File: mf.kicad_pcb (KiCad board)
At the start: 2 copper layers, 280 x 130 mm, 18 parts

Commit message: New schematic
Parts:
- added C2: Capacitor_NP, Capacitor_THT:C_Disc_D3.0mm_W2.0mm_P2.50mm, F.Cu at (496.1, 239.6)
- added C3: Capacitor_NP, Capacitor_THT:C_Disc_D3.0mm_W2.0mm_P2.50mm, F.Cu at (496.1, 243.2)
- added C4: Capacitor_NP, Capacitor_THT:C_Disc_D3.0mm_W2.0mm_P2.50mm, F.Cu at (547.9, 225.9)
- added C6: Capacitor_NP, Capacitor_THT:C_Disc_D3.0mm_W2.0mm_P2.50mm, F.Cu at (547.9, 229.4)
- added R17: Resistor, Resistor_THT:R_Axial_DIN0207_L6.3mm_D2.5mm_P10.16mm_Horizontal, F.Cu at (482.8, 218.0)
- added R18: Resistor, Resistor_THT:R_Axial_DIN0207_L6.3mm_D2.5mm_P10.16mm_Horizontal, F.Cu at (482.8, 222.1)
- added R19: Resistor, Resistor_THT:R_Axial_DIN0207_L6.3mm_D2.5mm_P10.16mm_Horizontal, F.Cu at (482.8, 226.1)
- added R20: Resistor, Resistor_THT:R_Axial_DIN0207_L6.3mm_D2.5mm_P10.16mm_Horizontal, F.Cu at (482.8, 230.2)
- added R21: Resistor, Resistor_THT:R_Axial_DIN0207_L6.3mm_D2.5mm_P10.16mm_Horizontal, F.Cu at (482.8, 234.2)
- added R22: Resistor, Resistor_THT:R_Axial_DIN0207_L6.3mm_D2.5mm_P10.16mm_Horizontal, F.Cu at (482.8, 238.3)
- added R23: Resistor, Resistor_THT:R_Axial_DIN0207_L6.3mm_D2.5mm_P10.16mm_Horizontal, F.Cu at (482.8, 242.3)
- added R24: Resistor, Resistor_THT:R_Axial_DIN0207_L6.3mm_D2.5mm_P10.16mm_Horizontal, F.Cu at (482.8, 246.4)
- added R25: Resistor, Resistor_THT:R_Axial_DIN0207_L6.3mm_D2.5mm_P10.16mm_Horizontal, F.Cu at (482.8, 250.4)
- added R26: Resistor, Resistor_THT:R_Axial_DIN0207_L6.3mm_D2.5mm_P10.16mm_Horizontal, F.Cu at (482.8, 254.5)
- added R27: Resistor, Resistor_THT:R_Axial_DIN0207_L6.3mm_D2.5mm_P10.16mm_Horizontal, F.Cu at (482.8, 258.5)
- added R28: Resistor, Resistor_THT:R_Axial_DIN0207_L6.3mm_D2.5mm_P10.16mm_Horizontal, F.Cu at (482.8, 262.6)
- added R29: Resistor, Resistor_THT:R_Axial_DIN0207_L6.3mm_D2.5mm_P10.16mm_Horizontal, F.Cu at (482.8, 266.6)
- added R30: Resistor, Resistor_THT:R_Axial_DIN0207_L6.3mm_D2.5mm_P10.16mm_Horizontal, F.Cu at (482.8, 270.7)
- added R31: Resistor, Resistor_THT:R_Axial_DIN0207_L6.3mm_D2.5mm_P10.16mm_Horizontal, F.Cu at (482.8, 274.7)
- added R32: Resistor, Resistor_THT:R_Axial_DIN0207_L6.3mm_D2.5mm_P10.16mm_Horizontal, F.Cu at (482.8, 278.8)
- added R33: R, Resistor_THT:R_Axial_DIN0207_L6.3mm_D2.5mm_P10.16mm_Horizontal, F.Cu at (547.9, 218.0)
- added R37: R, Resistor_THT:R_Axial_DIN0207_L6.3mm_D2.5mm_P10.16mm_Horizontal, F.Cu at (547.9, 222.1)
- added U11: DM13a, Package_DIP:DIP-24_W10.16mm, F.Cu at (534.6, 218.0)
- added U5: 74HC165, Package_DIP:DIP-16_W7.62mm_LongPads, F.Cu at (496.5, 218.0)
- added U6: 74HC165, Package_DIP:DIP-16_W7.62mm_LongPads, F.Cu at (508.1, 218.0)
- added U9: DM13a, Package_DIP:DIP-24_W10.16mm, F.Cu at (521.3, 218.0)
- U1: value ~ -> Sparkfun_Pro_Micro
- U4: footprint mf:RP2040-Zero -> mf:7seg_x8
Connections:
- BC1 pad 2: unconnected-(BC1-C-Pad2) -> GND
- BC1 pad 3: unconnected-(BC1-NO-Pad3) -> Net-(BC1-NO)
- BC1 pad 4: unconnected-(BC1-LED-Pad4) -> /Input/LED_BC1
- BC1 pad 5: unconnected-(BC1-GND-Pad5) -> +5V
- BC2 pad 2: unconnected-(BC2-C-Pad2) -> GND
- BC2 pad 3: unconnected-(BC2-NO-Pad3) -> Net-(BC2-NO)
- BC2 pad 4: unconnected-(BC2-LED-Pad4) -> /Input/LED_BC2
- BC2 pad 5: unconnected-(BC2-GND-Pad5) -> +5V
- BC3 pad 2: unconnected-(BC3-C-Pad2) -> GND
- BC3 pad 3: unconnected-(BC3-NO-Pad3) -> Net-(BC3-NO)
- BC3 pad 4: unconnected-(BC3-LED-Pad4) -> /Input/LED_BC3
- BC3 pad 5: unconnected-(BC3-GND-Pad5) -> +5V
- BC4 pad 2: unconnected-(BC4-C-Pad2) -> GND
- BC4 pad 3: unconnected-(BC4-NO-Pad3) -> Net-(BC4-NO)
- BC4 pad 4: unconnected-(BC4-LED-Pad4) -> /Input/LED_BC4
- BC4 pad 5: unconnected-(BC4-GND-Pad5) -> +5V
- BC5 pad 2: unconnected-(BC5-C-Pad2) -> GND
- BC5 pad 3: unconnected-(BC5-NO-Pad3) -> Net-(BC5-NO)
- BC5 pad 4: unconnected-(BC5-LED-Pad4) -> /Input/LED_BC5
- BC5 pad 5: unconnected-(BC5-GND-Pad5) -> +5V
- BC6 pad 2: unconnected-(BC6-C-Pad2) -> GND
- BC6 pad 3: unconnected-(BC6-NO-Pad3) -> Net-(BC6-NO)
- BC6 pad 4: unconnected-(BC6-LED-Pad4) -> /Input/LED_BC6
- BC6 pad 5: unconnected-(BC6-GND-Pad5) -> +5V
- BC7 pad 2: unconnected-(BC7-C-Pad2) -> GND
- BC7 pad 3: unconnected-(BC7-NO-Pad3) -> Net-(BC7-NO)
- BC7 pad 4: unconnected-(BC7-LED-Pad4) -> /Input/LED_BC7
- BC7 pad 5: unconnected-(BC7-GND-Pad5) -> +5V
- E1 pad 1: unconnected-(E1-A-Pad1) -> /Input/E1_A
- E1 pad 2: unconnected-(E1-COM-Pad2) -> GND
- E1 pad 3: unconnected-(E1-B-Pad3) -> /Input/E1_B
- E1 pad 4: unconnected-(E1-D-Pad4) -> Net-(E1-D)
- E1 pad 5: unconnected-(E1-E-Pad5) -> GND
- E2 pad 1: unconnected-(E2-A-Pad1) -> /Input/E2_A
- E2 pad 2: unconnected-(E2-COM-Pad2) -> GND
- E2 pad 3: unconnected-(E2-B-Pad3) -> /Input/E2_B
- E2 pad 4: unconnected-(E2-D-Pad4) -> Net-(E2-D)
- E2 pad 5: unconnected-(E2-E-Pad5) -> GND
- E3 pad 1: unconnected-(E3-A-Pad1) -> /Input/E3_A
- E3 pad 2: unconnected-(E3-COM-Pad2) -> GND
- E3 pad 3: unconnected-(E3-B-Pad3) -> /Input/E3_B
- E3 pad 4: unconnected-(E3-D-Pad4) -> Net-(E3-D)
- E3 pad 5: unconnected-(E3-E-Pad5) -> GND
- E4 pad 1: unconnected-(E4-A-Pad1) -> /Input/E4_A
- E4 pad 2: unconnected-(E4-COM-Pad2) -> GND
- E4 pad 3: unconnected-(E4-B-Pad3) -> /Input/E4_B
- E4 pad 4: unconnected-(E4-D-Pad4) -> Net-(E4-D)
- E4 pad 5: unconnected-(E4-E-Pad5) -> GND
- RB1 pad 1: unconnected-(RB1-Pad1) -> GND
- RB1 pad 2: unconnected-(RB1-Pad2) -> Net-(U6-D3)
- RB2 pad 1: unconnected-(RB2-Pad1) -> GND
- RB2 pad 2: unconnected-(RB2-Pad2) -> Net-(U6-D2)
- RB3 pad 1: unconnected-(RB3-Pad1) -> GND
- RB3 pad 2: unconnected-(RB3-Pad2) -> Net-(U6-D1)
- U1 pad 3: unconnected-(U1-D2-Pad3) -> GND
- U1 pad 4: unconnected-(U1-GND-Pad4) -> GND
- U2 pad 1: unconnected-(U2-5V-Pad1) -> +5V
- U2 pad 2: unconnected-(U2-D1-Pad2) -> GND
- U2 pad 3: unconnected-(U2-D2-Pad3) -> /Output/O_8_DIN
- U2 pad 4: unconnected-(U2-GND-Pad4) -> /Output/O_8_CS
- U3 pad 1: unconnected-(U3-5V-Pad1) -> /Output/O_4_CLK
- U3 pad 10: unconnected-(U3-GP0-Pad10) -> (no net)
- U3 pad 11: unconnected-(U3-GP1-Pad11) -> (no net)
- U3 pad 12: unconnected-(U3-GP2-Pad12) -> (no net)
- U3 pad 13: unconnected-(U3-GP3-Pad13) -> (no net)
- U3 pad 14: unconnected-(U3-GP4-Pad14) -> (no net)
- U3 pad 15: unconnected-(U3-GP5-Pad15) -> (no net)
- U3 pad 16: unconnected-(U3-GP6-Pad16) -> (no net)
- U3 pad 17: unconnected-(U3-GP7-Pad17) -> (no net)
- U3 pad 18: unconnected-(U3-GP8-Pad18) -> (no net)
- U3 pad 19: unconnected-(U3-GP13-Pad19) -> (no net)
- U3 pad 2: unconnected-(U3-GND-Pad2) -> /Output/O_4_DIN
- U3 pad 20: unconnected-(U3-GP12-Pad20) -> (no net)
- U3 pad 21: unconnected-(U3-GP11-Pad21) -> (no net)
- U3 pad 22: unconnected-(U3-GP10-Pad22) -> (no net)
- U3 pad 23: unconnected-(U3-GP9-Pad23) -> (no net)
- U3 pad 3: unconnected-(U3-3V3-Pad3) -> +5V
- U3 pad 4: unconnected-(U3-GP29-Pad4) -> GND
- U3 pad 5: unconnected-(U3-GP28-Pad5) -> (no net)
- U3 pad 6: unconnected-(U3-GP27-Pad6) -> (no net)
- U3 pad 7: unconnected-(U3-GP26-Pad7) -> (no net)
- U3 pad 8: unconnected-(U3-GP15-Pad8) -> (no net)
- U3 pad 9: unconnected-(U3-GP14-Pad9) -> (no net)
- U4 pad 1: unconnected-(U4-5V-Pad1) -> +5V
- U4 pad 2: unconnected-(U4-GND-Pad2) -> GND
- U4 pad 3: unconnected-(U4-3V3-Pad3) -> Net-(U2-DOUT)
- U4 pad 4: unconnected-(U4-GP29-Pad4) -> Net-(U2-LODA)

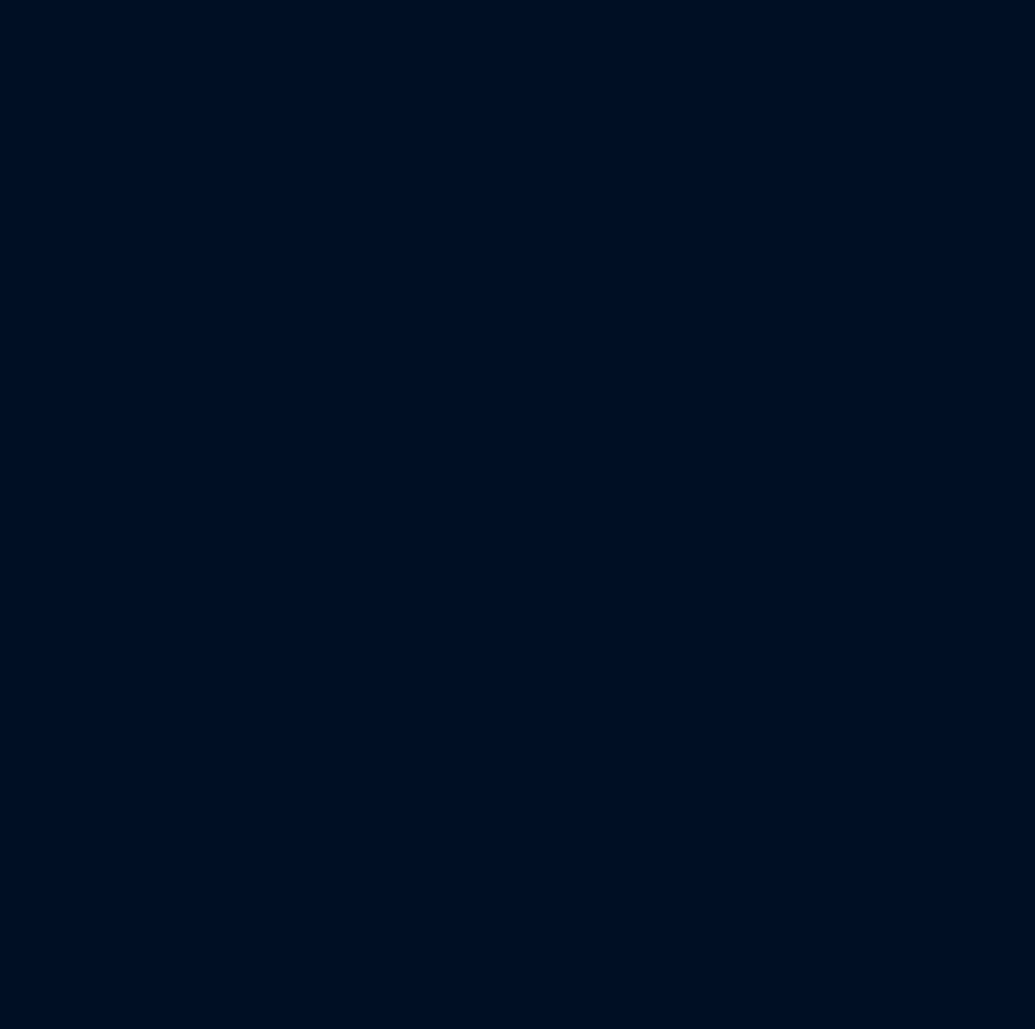
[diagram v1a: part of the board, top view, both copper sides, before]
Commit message: Update schematic with nearly everything
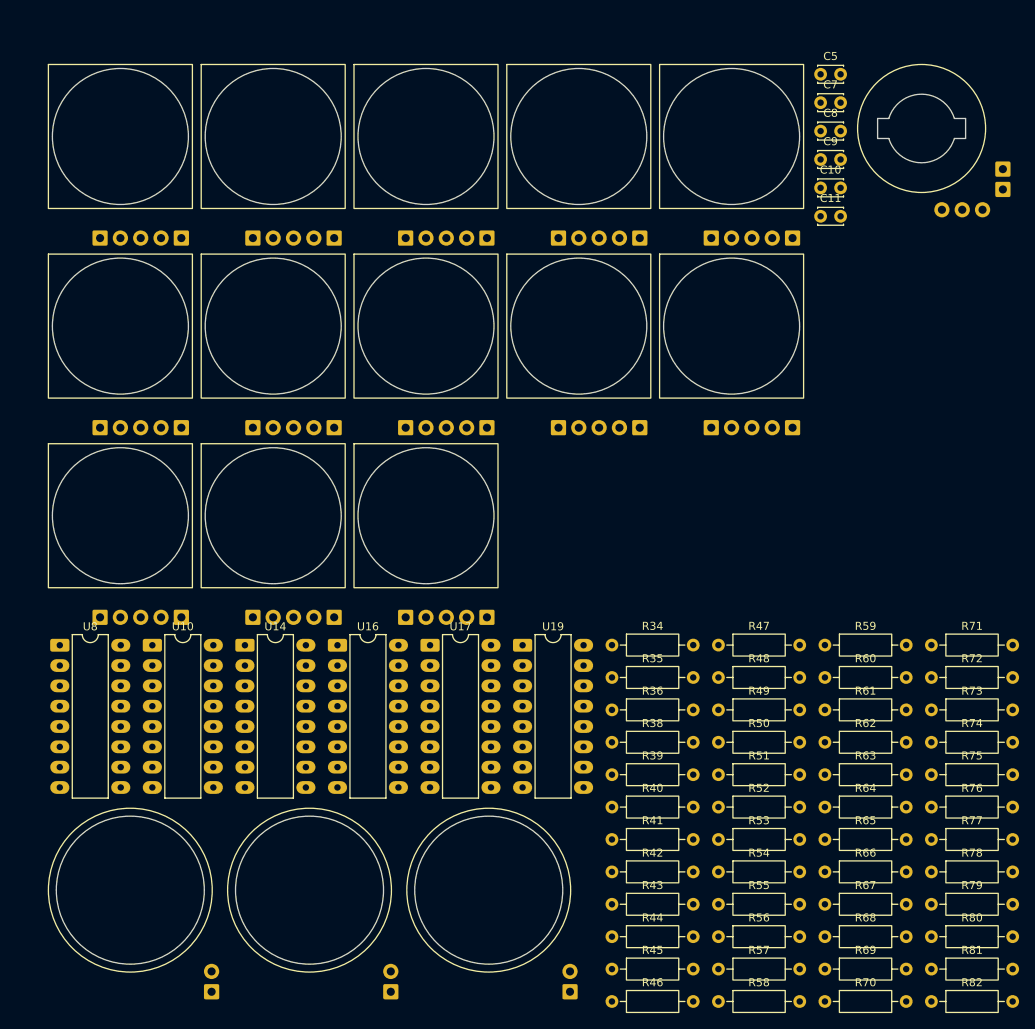
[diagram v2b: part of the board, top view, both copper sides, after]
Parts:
- added BC10: ~, mf:sq_but, F.Cu at (513.8, 346.3)
- added BC11: ~, mf:sq_but, F.Cu at (532.9, 346.3)
- added BC12: ~, mf:sq_but, F.Cu at (552.0, 346.3)
- added BC13: ~, mf:sq_but, F.Cu at (475.6, 370.0)
- added BC14: ~, mf:sq_but, F.Cu at (494.6, 370.0)
- added BC15: ~, mf:sq_but, F.Cu at (513.8, 370.0)
- added BC16: ~, mf:sq_but, F.Cu at (532.9, 370.0)
- added BC17: ~, mf:sq_but, F.Cu at (552.0, 370.0)
- added BC18: ~, mf:sq_but, F.Cu at (475.6, 393.7)
- added BC19: ~, mf:sq_but, F.Cu at (494.6, 393.7)
- added BC20: ~, mf:sq_but, F.Cu at (513.8, 393.7)
- added BC8: ~, mf:sq_but, F.Cu at (475.6, 346.3)
- added BC9: ~, mf:sq_but, F.Cu at (494.6, 346.3)
- added C10: Capacitor_NP, Capacitor_THT:C_Disc_D3.0mm_W2.0mm_P2.50mm, F.Cu at (563.1, 352.7)
- added C11: Capacitor_NP, Capacitor_THT:C_Disc_D3.0mm_W2.0mm_P2.50mm, F.Cu at (563.1, 356.3)
- added C5: Capacitor_NP, Capacitor_THT:C_Disc_D3.0mm_W2.0mm_P2.50mm, F.Cu at (563.1, 338.5)
- added C7: Capacitor_NP, Capacitor_THT:C_Disc_D3.0mm_W2.0mm_P2.50mm, F.Cu at (563.1, 342.1)
- added C8: Capacitor_NP, Capacitor_THT:C_Disc_D3.0mm_W2.0mm_P2.50mm, F.Cu at (563.1, 345.6)
- added C9: Capacitor_NP, Capacitor_THT:C_Disc_D3.0mm_W2.0mm_P2.50mm, F.Cu at (563.1, 349.2)
- added E5: ~, mf:ec11-ext, F.Cu at (575.7, 345.3)
- added R34: Resistor, Resistor_THT:R_Axial_DIN0207_L6.3mm_D2.5mm_P10.16mm_Horizontal, F.Cu at (537.0, 409.9)
- added R35: Resistor, Resistor_THT:R_Axial_DIN0207_L6.3mm_D2.5mm_P10.16mm_Horizontal, F.Cu at (537.0, 413.9)
- added R36: Resistor, Resistor_THT:R_Axial_DIN0207_L6.3mm_D2.5mm_P10.16mm_Horizontal, F.Cu at (537.0, 418.0)
- added R38: Resistor, Resistor_THT:R_Axial_DIN0207_L6.3mm_D2.5mm_P10.16mm_Horizontal, F.Cu at (537.0, 422.0)
- added R39: Resistor, Resistor_THT:R_Axial_DIN0207_L6.3mm_D2.5mm_P10.16mm_Horizontal, F.Cu at (537.0, 426.1)
- added R40: Resistor, Resistor_THT:R_Axial_DIN0207_L6.3mm_D2.5mm_P10.16mm_Horizontal, F.Cu at (537.0, 430.1)
- added R41: Resistor, Resistor_THT:R_Axial_DIN0207_L6.3mm_D2.5mm_P10.16mm_Horizontal, F.Cu at (537.0, 434.2)
- added R42: Resistor, Resistor_THT:R_Axial_DIN0207_L6.3mm_D2.5mm_P10.16mm_Horizontal, F.Cu at (537.0, 438.2)
- added R43: Resistor, Resistor_THT:R_Axial_DIN0207_L6.3mm_D2.5mm_P10.16mm_Horizontal, F.Cu at (537.0, 442.3)
- added R44: Resistor, Resistor_THT:R_Axial_DIN0207_L6.3mm_D2.5mm_P10.16mm_Horizontal, F.Cu at (537.0, 446.3)
- added R45: Resistor, Resistor_THT:R_Axial_DIN0207_L6.3mm_D2.5mm_P10.16mm_Horizontal, F.Cu at (537.0, 450.4)
- added R46: Resistor, Resistor_THT:R_Axial_DIN0207_L6.3mm_D2.5mm_P10.16mm_Horizontal, F.Cu at (537.0, 454.4)
- added R47: Resistor, Resistor_THT:R_Axial_DIN0207_L6.3mm_D2.5mm_P10.16mm_Horizontal, F.Cu at (550.3, 409.9)
- added R48: Resistor, Resistor_THT:R_Axial_DIN0207_L6.3mm_D2.5mm_P10.16mm_Horizontal, F.Cu at (550.3, 413.9)
- added R49: Resistor, Resistor_THT:R_Axial_DIN0207_L6.3mm_D2.5mm_P10.16mm_Horizontal, F.Cu at (550.3, 418.0)
- added R50: Resistor, Resistor_THT:R_Axial_DIN0207_L6.3mm_D2.5mm_P10.16mm_Horizontal, F.Cu at (550.3, 422.0)
- added R51: Resistor, Resistor_THT:R_Axial_DIN0207_L6.3mm_D2.5mm_P10.16mm_Horizontal, F.Cu at (550.3, 426.1)
- added R52: Resistor, Resistor_THT:R_Axial_DIN0207_L6.3mm_D2.5mm_P10.16mm_Horizontal, F.Cu at (550.3, 430.1)
- added R53: Resistor, Resistor_THT:R_Axial_DIN0207_L6.3mm_D2.5mm_P10.16mm_Horizontal, F.Cu at (550.3, 434.2)
- added R54: Resistor, Resistor_THT:R_Axial_DIN0207_L6.3mm_D2.5mm_P10.16mm_Horizontal, F.Cu at (550.3, 438.2)
- added R55: Resistor, Resistor_THT:R_Axial_DIN0207_L6.3mm_D2.5mm_P10.16mm_Horizontal, F.Cu at (550.3, 442.3)
- added R56: Resistor, Resistor_THT:R_Axial_DIN0207_L6.3mm_D2.5mm_P10.16mm_Horizontal, F.Cu at (550.3, 446.3)
- added R57: Resistor, Resistor_THT:R_Axial_DIN0207_L6.3mm_D2.5mm_P10.16mm_Horizontal, F.Cu at (550.3, 450.4)
- added R58: Resistor, Resistor_THT:R_Axial_DIN0207_L6.3mm_D2.5mm_P10.16mm_Horizontal, F.Cu at (550.3, 454.4)
- added R59: Resistor, Resistor_THT:R_Axial_DIN0207_L6.3mm_D2.5mm_P10.16mm_Horizontal, F.Cu at (563.6, 409.9)
- added R60: Resistor, Resistor_THT:R_Axial_DIN0207_L6.3mm_D2.5mm_P10.16mm_Horizontal, F.Cu at (563.6, 413.9)
- added R61: Resistor, Resistor_THT:R_Axial_DIN0207_L6.3mm_D2.5mm_P10.16mm_Horizontal, F.Cu at (563.6, 418.0)
- added R62: Resistor, Resistor_THT:R_Axial_DIN0207_L6.3mm_D2.5mm_P10.16mm_Horizontal, F.Cu at (563.6, 422.0)
- added R63: Resistor, Resistor_THT:R_Axial_DIN0207_L6.3mm_D2.5mm_P10.16mm_Horizontal, F.Cu at (563.6, 426.1)
- added R64: Resistor, Resistor_THT:R_Axial_DIN0207_L6.3mm_D2.5mm_P10.16mm_Horizontal, F.Cu at (563.6, 430.1)
- added R65: Resistor, Resistor_THT:R_Axial_DIN0207_L6.3mm_D2.5mm_P10.16mm_Horizontal, F.Cu at (563.6, 434.2)
- added R66: Resistor, Resistor_THT:R_Axial_DIN0207_L6.3mm_D2.5mm_P10.16mm_Horizontal, F.Cu at (563.6, 438.2)
- added R67: Resistor, Resistor_THT:R_Axial_DIN0207_L6.3mm_D2.5mm_P10.16mm_Horizontal, F.Cu at (563.6, 442.3)
- added R68: Resistor, Resistor_THT:R_Axial_DIN0207_L6.3mm_D2.5mm_P10.16mm_Horizontal, F.Cu at (563.6, 446.3)
- added R69: Resistor, Resistor_THT:R_Axial_DIN0207_L6.3mm_D2.5mm_P10.16mm_Horizontal, F.Cu at (563.6, 450.4)
- added R70: Resistor, Resistor_THT:R_Axial_DIN0207_L6.3mm_D2.5mm_P10.16mm_Horizontal, F.Cu at (563.6, 454.4)
- added R71: Resistor, Resistor_THT:R_Axial_DIN0207_L6.3mm_D2.5mm_P10.16mm_Horizontal, F.Cu at (576.9, 409.9)
- added R72: Resistor, Resistor_THT:R_Axial_DIN0207_L6.3mm_D2.5mm_P10.16mm_Horizontal, F.Cu at (576.9, 413.9)
- added R73: Resistor, Resistor_THT:R_Axial_DIN0207_L6.3mm_D2.5mm_P10.16mm_Horizontal, F.Cu at (576.9, 418.0)
- added R74: Resistor, Resistor_THT:R_Axial_DIN0207_L6.3mm_D2.5mm_P10.16mm_Horizontal, F.Cu at (576.9, 422.0)
- added R75: Resistor, Resistor_THT:R_Axial_DIN0207_L6.3mm_D2.5mm_P10.16mm_Horizontal, F.Cu at (576.9, 426.1)
- added R76: Resistor, Resistor_THT:R_Axial_DIN0207_L6.3mm_D2.5mm_P10.16mm_Horizontal, F.Cu at (576.9, 430.1)
- added R77: Resistor, Resistor_THT:R_Axial_DIN0207_L6.3mm_D2.5mm_P10.16mm_Horizontal, F.Cu at (576.9, 434.2)
- added R78: Resistor, Resistor_THT:R_Axial_DIN0207_L6.3mm_D2.5mm_P10.16mm_Horizontal, F.Cu at (576.9, 438.2)
- added R79: Resistor, Resistor_THT:R_Axial_DIN0207_L6.3mm_D2.5mm_P10.16mm_Horizontal, F.Cu at (576.9, 442.3)
- added R80: Resistor, Resistor_THT:R_Axial_DIN0207_L6.3mm_D2.5mm_P10.16mm_Horizontal, F.Cu at (576.9, 446.3)
- added R81: Resistor, Resistor_THT:R_Axial_DIN0207_L6.3mm_D2.5mm_P10.16mm_Horizontal, F.Cu at (576.9, 450.4)
- added R82: Resistor, Resistor_THT:R_Axial_DIN0207_L6.3mm_D2.5mm_P10.16mm_Horizontal, F.Cu at (576.9, 454.4)
- added RB4: ~, mf:r_but, F.Cu at (476.8, 440.5)
- added RB5: ~, mf:r_but, F.Cu at (499.2, 440.5)
- added RB6: ~, mf:r_but, F.Cu at (521.6, 440.5)
- added U10: 74HC165, Package_DIP:DIP-16_W7.62mm_LongPads, F.Cu at (479.5, 409.9)
- added U14: 74HC165, Package_DIP:DIP-16_W7.62mm_LongPads, F.Cu at (491.1, 409.9)
- added U16: 74HC165, Package_DIP:DIP-16_W7.62mm_LongPads, F.Cu at (502.7, 409.9)
- added U17: 74HC165, Package_DIP:DIP-16_W7.62mm_LongPads, F.Cu at (514.3, 409.9)
- added U19: 74HC165, Package_DIP:DIP-16_W7.62mm_LongPads, F.Cu at (525.8, 409.9)
- added U8: 74HC165, Package_DIP:DIP-16_W7.62mm_LongPads, F.Cu at (468.0, 409.9)
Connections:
- BC1 pad 2: GND -> Net-(BC1-C)
- BC2 pad 2: GND -> Net-(BC1-C)
- BC3 pad 2: GND -> Net-(BC1-C)
- BC4 pad 2: GND -> Net-(BC1-C)
- BC5 pad 2: GND -> Net-(BC1-C)
- BC6 pad 2: GND -> Net-(BC1-C)
- BC7 pad 2: GND -> Net-(BC1-C)
- R21 pad 2: Net-(BC7-NO) -> Net-(U5-D4)
- R22 pad 2: Net-(BC6-NO) -> Net-(U5-D5)
- R23 pad 2: Net-(BC5-NO) -> Net-(U5-D6)
- R24 pad 2: Net-(BC4-NO) -> Net-(BC15-NO)
- R25 pad 2: Net-(BC3-NO) -> Net-(BC16-NO)
- R26 pad 2: Net-(U6-D1) -> Net-(BC17-NO)
- R27 pad 2: Net-(U6-D2) -> Net-(BC18-NO)
- R28 pad 2: Net-(U6-D3) -> Net-(BC19-NO)
- R29 pad 2: Net-(BC2-NO) -> Net-(BC20-NO)
- R30 pad 2: Net-(BC1-NO) -> Net-(U6-D5)
- U11 pad 5: unconnected-(U11-OUT0-Pad5) -> /Input/LED_BC17
- U11 pad 6: unconnected-(U11-OUT1-Pad6) -> /Input/LED_BC18
- U11 pad 7: unconnected-(U11-OUT2-Pad7) -> /Input/LED_BC19
- U11 pad 8: unconnected-(U11-OUT3-Pad8) -> /Input/LED_BC20
- U5 pad 3: Net-(BC7-NO) -> Net-(U5-D4)
- U5 pad 4: Net-(BC6-NO) -> Net-(U5-D5)
- U5 pad 5: Net-(BC5-NO) -> Net-(U5-D6)
- U5 pad 6: Net-(BC4-NO) -> Net-(BC15-NO)
- U6 pad 11: Net-(BC3-NO) -> Net-(BC16-NO)
- U6 pad 12: Net-(U6-D1) -> Net-(BC17-NO)
- U6 pad 13: Net-(U6-D2) -> Net-(BC18-NO)
- U6 pad 14: Net-(U6-D3) -> Net-(BC19-NO)
- U6 pad 3: Net-(BC2-NO) -> Net-(BC20-NO)
- U6 pad 4: Net-(BC1-NO) -> Net-(U6-D5)
- U6 pad 9: /Input/I_DATA_R -> Net-(U6-Q7)
- U9 pad 10: unconnected-(U9-OUT5-Pad10) -> /Input/LED_BC6
- U9 pad 11: unconnected-(U9-OUT6-Pad11) -> /Input/LED_BC7
- U9 pad 12: unconnected-(U9-OUT7-Pad12) -> /Input/LED_BC8
- U9 pad 13: unconnected-(U9-OUT8-Pad13) -> /Input/LED_BC9
- U9 pad 14: /Input/LED_BC1 -> /Input/LED_BC10
- U9 pad 15: /Input/LED_BC2 -> /Input/LED_BC11
- U9 pad 16: /Input/LED_BC3 -> /Input/LED_BC12
- U9 pad 17: /Input/LED_BC4 -> /Input/LED_BC13
- U9 pad 18: /Input/LED_BC5 -> /Input/LED_BC14
- U9 pad 19: /Input/LED_BC6 -> /Input/LED_BC15
- U9 pad 20: /Input/LED_BC7 -> /Input/LED_BC16
- U9 pad 5: unconnected-(U9-OUT0-Pad5) -> /Input/LED_BC1
- U9 pad 6: unconnected-(U9-OUT1-Pad6) -> /Input/LED_BC2
- U9 pad 7: unconnected-(U9-OUT2-Pad7) -> /Input/LED_BC3
- U9 pad 8: unconnected-(U9-OUT3-Pad8) -> /Input/LED_BC4
- U9 pad 9: unconnected-(U9-OUT4-Pad9) -> /Input/LED_BC5

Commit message: New pcb and 3 pos switch footprint
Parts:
- removed C11: Capacitor_NP, Capacitor_THT:C_Disc_D3.0mm_W2.0mm_P2.50mm
- removed RB1, RB2, RB3: ~, mf:r_but
- removed U3: ~, mf:RP2040-Zero
- added C1: Capacitor_NP, Capacitor_THT:C_Disc_D3.0mm_W2.0mm_P2.50mm, B.Cu at (136.2, 196.5)
- added U15: ~, mf:3posswitch, F.Cu at (34.5, 169.1)
- added U18: ~, mf:3posswitch, F.Cu at (34.5, 179.9)
- added U20: ~, mf:3posswitch, F.Cu at (126.2, 80.2)
- added U7: Sparkfun_Pro_Micro, Arduino:Sparkfun_Pro_Micro, F.Cu at (334.7, 93.9)
- C10, C2, C3, C4, C5, C6, C7, C8, C9, R17, R18, R19, R20, R21, R22, R23, R24, R25, R26, R27, R28, R29, R30, R31, R32, R33, R34, R35, R36, R37, R38, R39, R40, R41, R42, R43, R44, R45, R46, R47, R48, R49, R50, R51, R52, R53, R54, R55, R56, R57, R58, R59, R60, R61, R62, R63, R64, R65, R66, R67, R68, R69, R70, R71, R72, R73, R74, R75, R76, R77, R78, R79, R80, R81, R82, U10, U11, U14, U16, U17, U19, U5, U6, U8, U9: moved to B.Cu
- U1: footprint mf:7seg_x8 -> Arduino:Sparkfun_Pro_Micro
- U4: moved to F.Cu
- moved R70 591.2 mm to (72.6, 125.1)
- moved R69 587.3 mm to (72.6, 128.1)
- moved R68 583.5 mm to (72.6, 131.1)
- moved R67 579.7 mm to (72.6, 134.1)
- moved R74 548.3 mm to (110.3, 134.1), turned to 180 degrees
- moved R73 547.8 mm to (110.3, 131.1), turned to 180 degrees
- moved R72 547.2 mm to (110.3, 128.1), turned to 180 degrees
- moved R71 546.7 mm to (110.3, 125.1), turned to 180 degrees
- moved BC15 545.0 mm to (34.5, 110.5), turned to -90 degrees
- moved BC12 542.2 mm to (54.5, 130.5), turned to 90 degrees
- moved BC11 535.5 mm to (34.5, 150.4), turned to -90 degrees
- moved E5 523.2 mm to (88.5, 154.5), turned to 180 degrees
- moved R66 521.5 mm to (108.7, 183.2)
- moved R65 518.1 mm to (108.7, 186.2)
- moved R64 514.8 mm to (108.7, 189.2)
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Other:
- board size 280 x 130 mm -> 363 x 166.2 mm
- board text removed: "100"
- board text removed: "1000"
- board text removed: "ALT |-LVL"
- board text removed: "APPR"
- board text removed: "CH-| V/S FPA"
- board text removed: "DN"
- board text removed: "EXPED"
- board text removed: "HDG TRK LAT"
- board text removed: "METRIC ALT"
- board text removed: "SPD MACH"
- board text removed: "UP"
